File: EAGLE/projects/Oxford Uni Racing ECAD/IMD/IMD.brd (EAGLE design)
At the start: 59.7 x 44.5 mm, 7 parts, among them IC1 LM2901N, K1 RT444012

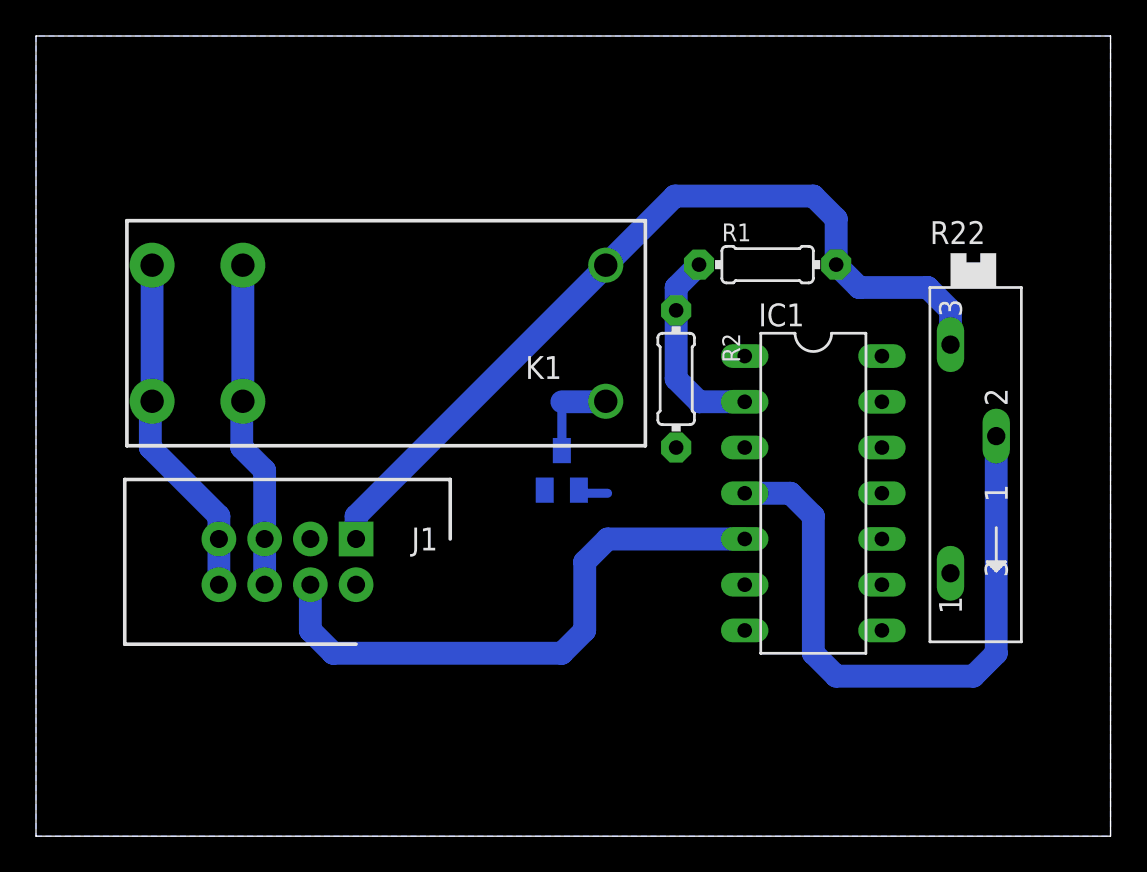
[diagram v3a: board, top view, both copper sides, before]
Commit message: replaced fuses with correct sized ones
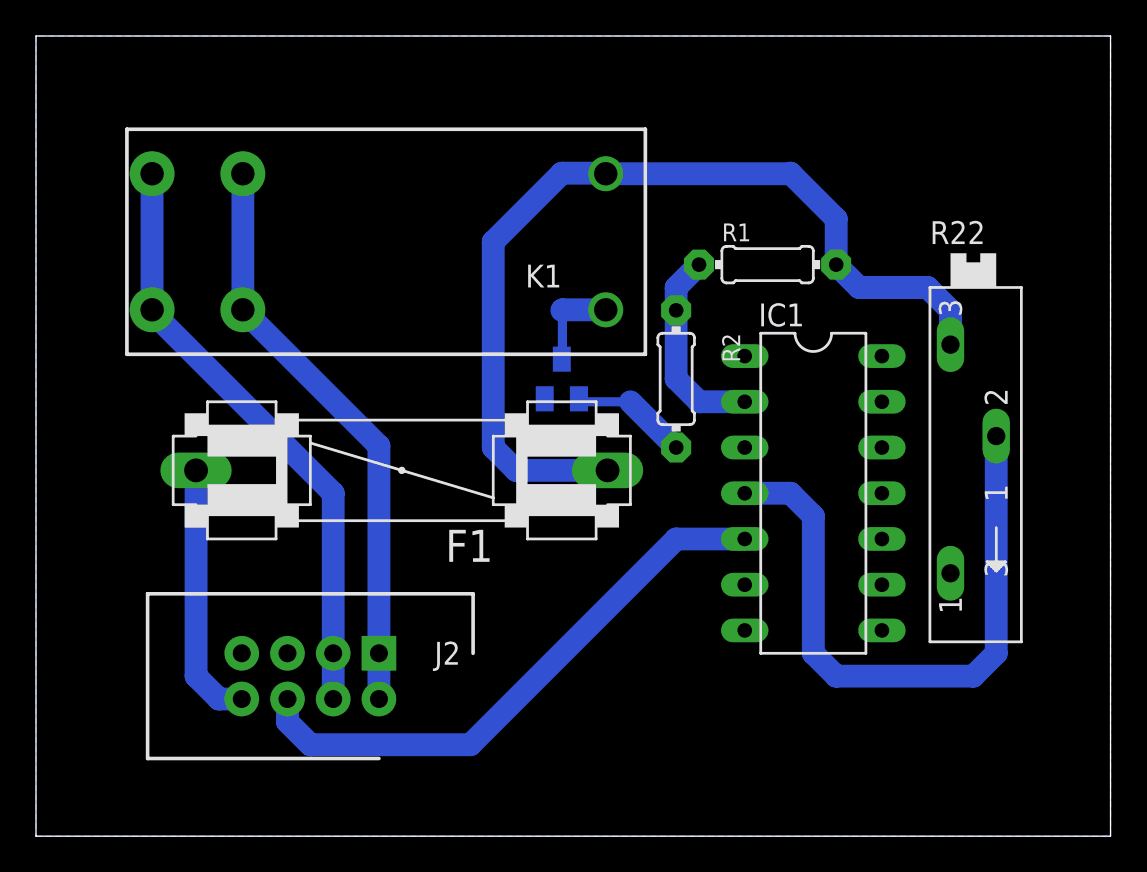
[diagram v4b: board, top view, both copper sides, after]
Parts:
- removed J1: (no value), T821108A1S100CEU:HDRV8W64P254_2X4_1778X895X915P
- added F1: 1A, special:FUSE
- added J2: (no value), T821108A1S100CEU:HDRV8W64P254_2X4_1778X895X915P
- moved K1 5.08 mm to (19.1, 33.0)
- moved BR_LIGHTS_TR 5.08 mm to (29.2, 25.4)
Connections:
- new net N$2: F1.2, J2.8
- net 12V: now also F1.1; no longer J1.1
- net ASS1: now also J2.1, J2.2, K1.11, K1.21; no longer J1.7, J1.8, K1.14, K1.24
- net ASS2: now also J2.3, J2.4, K1.14, K1.24; no longer J1.5, J1.6, K1.11, K1.21
- net GND: now also J2.7; no longer J1.2
- net IMD_REF: now also J2.6; no longer J1.4
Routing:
- net ASS2: track 18.3 -> 33.3 mm
- net N$2: track 0.00 -> 14.5 mm
- net ASS1: track 19.4 -> 32.3 mm
- net N$3: track 1.66 -> 6.52 mm
- net 12V: track 47.7 -> 51.9 mm
